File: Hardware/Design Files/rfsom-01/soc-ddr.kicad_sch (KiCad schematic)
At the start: 1 part

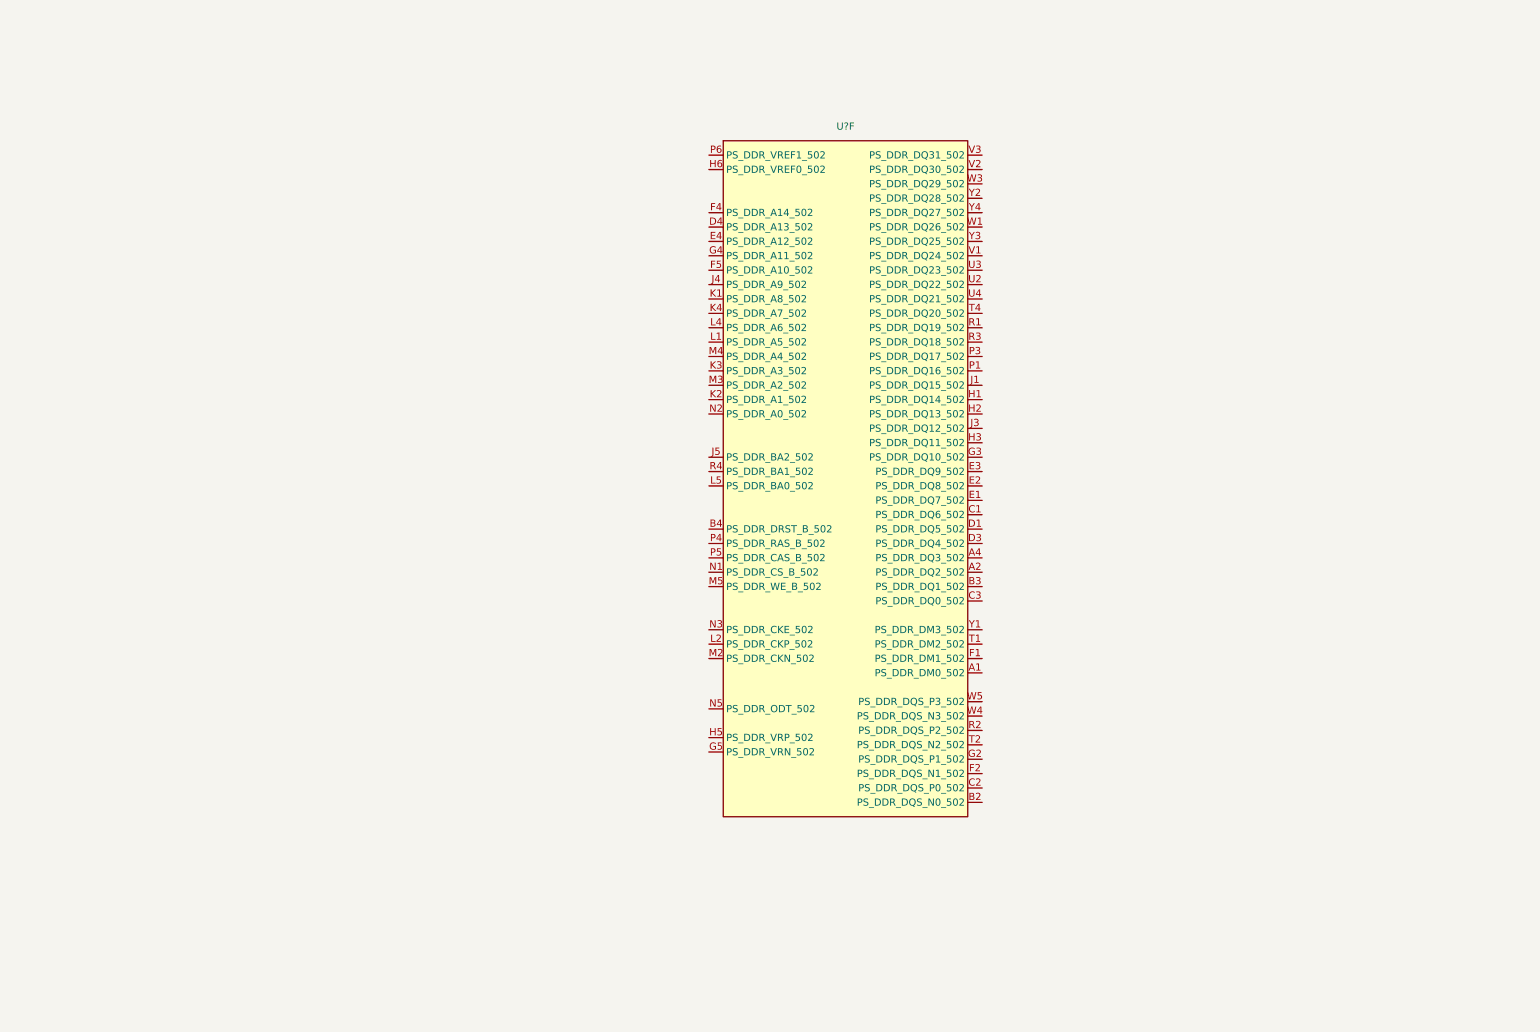
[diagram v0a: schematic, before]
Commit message: ddr progress; added more conns;
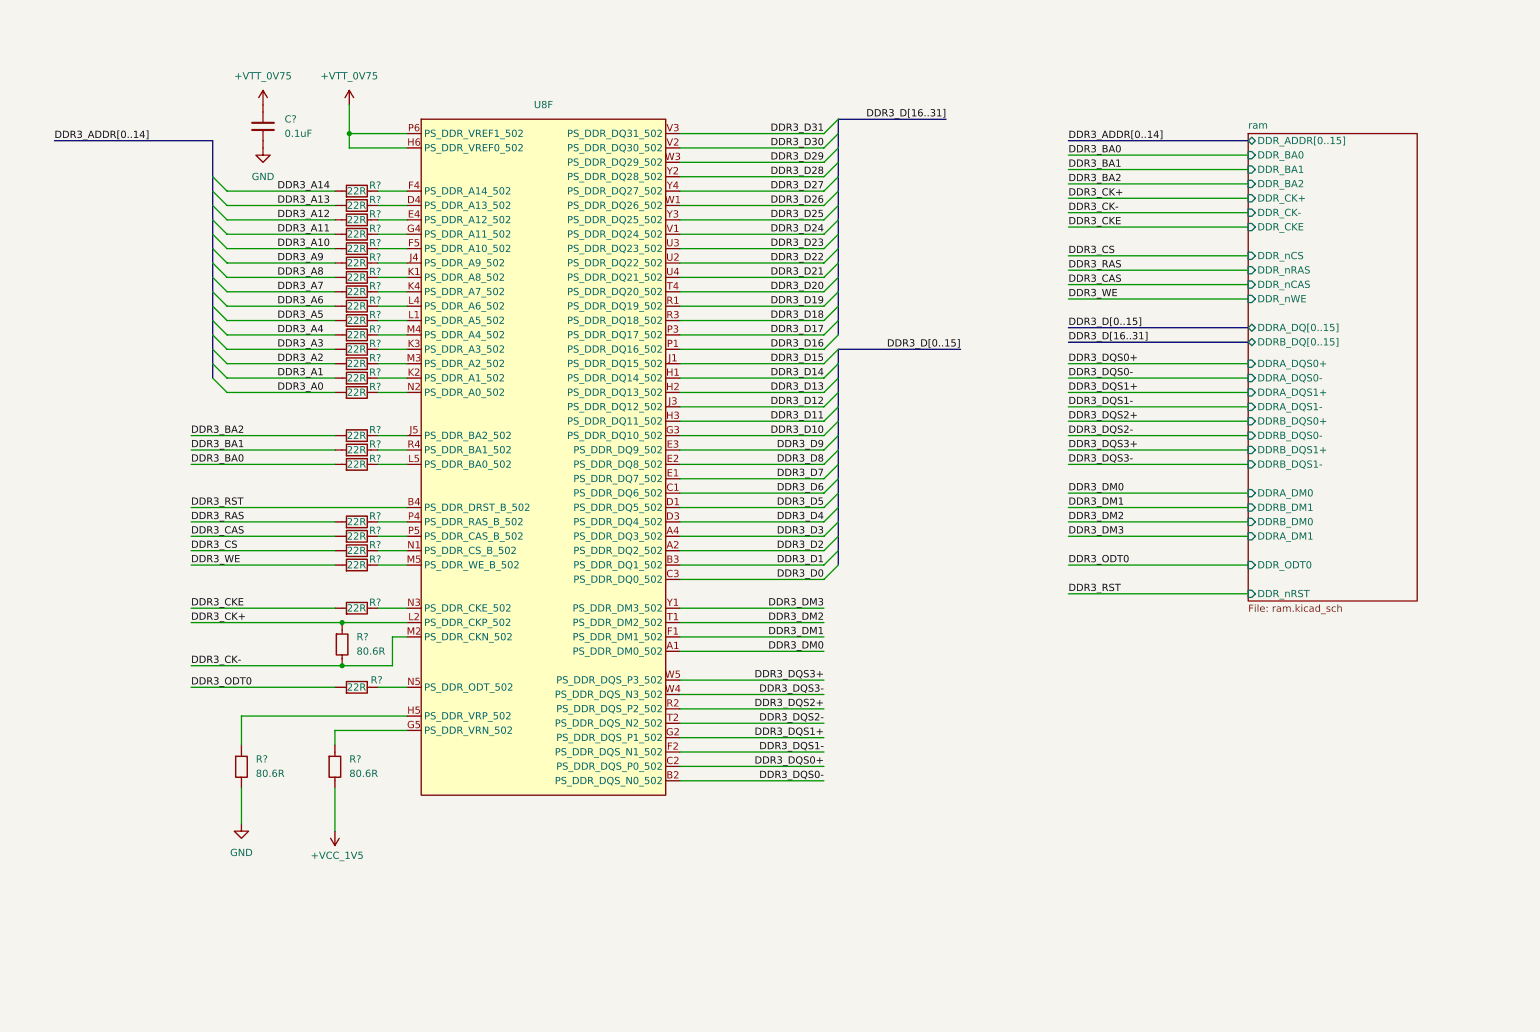
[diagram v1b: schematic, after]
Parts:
- added C?: CL05B104KA5NNNC, Capacitor_SMD:C_0402_1005Metric_Pad0.74x0.62mm_HandSolder, symbol Capacitors:CL05B104KA5NNNC
- added R? (x24): RC0402FR-0722RL, Resistor_SMD:R_0402_1005Metric, symbol Resistors:RC0402FR-0722RL
- added R? (x3): RC0402FR-0780R6L, Resistor_SMD:R_0402_1005Metric, symbol Resistors:RC0402FR-0780R6L
- U8: renamed from U?; footprint Package_BGA:Xilinx_CLG400 -> ICs:CLG400
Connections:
- net DDR3_DM0: now reaches U8.A1 (PS_DDR_DM0_502)
- net DDR3_D2: now reaches U8.A2 (PS_DDR_DQ2_502)
- net DDR3_D3: now reaches U8.A4 (PS_DDR_DQ3_502)
- net DDR3_DQS0-: now reaches U8.B2 (PS_DDR_DQS_N0_502)
- net DDR3_D1: now reaches U8.B3 (PS_DDR_DQ1_502)
- net DDR3_RST: now reaches U8.B4 (PS_DDR_DRST_B_502)
- net DDR3_D6: now reaches U8.C1 (PS_DDR_DQ6_502)
- net DDR3_DQS0+: now reaches U8.C2 (PS_DDR_DQS_P0_502)
- net DDR3_D0: now reaches U8.C3 (PS_DDR_DQ0_502)
- net DDR3_D5: now reaches U8.D1 (PS_DDR_DQ5_502)
- net DDR3_D4: now reaches U8.D3 (PS_DDR_DQ4_502)
- net at U8.D4 (PS_DDR_A13_502): now also R?.2
- net DDR3_D7: now reaches U8.E1 (PS_DDR_DQ7_502)
- net DDR3_D8: now reaches U8.E2 (PS_DDR_DQ8_502)
- net DDR3_D9: now reaches U8.E3 (PS_DDR_DQ9_502)
- net at U8.E4 (PS_DDR_A12_502): now also R?.2
- net DDR3_DM1: now reaches U8.F1 (PS_DDR_DM1_502)
- net DDR3_DQS1-: now reaches U8.F2 (PS_DDR_DQS_N1_502)
- net at U8.F4 (PS_DDR_A14_502): now also R?.2
- net at U8.F5 (PS_DDR_A10_502): now also R?.2
- net DDR3_DQS1+: now reaches U8.G2 (PS_DDR_DQS_P1_502)
- net DDR3_D10: now reaches U8.G3 (PS_DDR_DQ10_502)
- net at U8.G4 (PS_DDR_A11_502): now also R?.2
- net at U8.G5 (PS_DDR_VRN_502): now also R?.1
- net DDR3_D14: now reaches U8.H1 (PS_DDR_DQ14_502)
- net DDR3_D13: now reaches U8.H2 (PS_DDR_DQ13_502)
- net DDR3_D11: now reaches U8.H3 (PS_DDR_DQ11_502)
- net at U8.H5 (PS_DDR_VRP_502): now also R?.1
- net +VTT_0V75: now reaches U8.H6 (PS_DDR_VREF0_502)
- net +VTT_0V75: now also U8.P6 (PS_DDR_VREF1_502), C?.1
- net DDR3_D15: now reaches U8.J1 (PS_DDR_DQ15_502)
- net DDR3_D12: now reaches U8.J3 (PS_DDR_DQ12_502)
- net at U8.J4 (PS_DDR_A9_502): now also R?.2
- net at U8.J5 (PS_DDR_BA2_502): now also R?.2
- net at U8.K1 (PS_DDR_A8_502): now also R?.2
- net at U8.K2 (PS_DDR_A1_502): now also R?.2
- net at U8.K3 (PS_DDR_A3_502): now also R?.2
- net at U8.K4 (PS_DDR_A7_502): now also R?.2
- net at U8.L1 (PS_DDR_A5_502): now also R?.2
- net DDR3_CK+: now reaches U8.L2 (PS_DDR_CKP_502)
- net DDR3_CK+: now also R?.1
- net at U8.L4 (PS_DDR_A6_502): now also R?.2
- net at U8.L5 (PS_DDR_BA0_502): now also R?.2
- net DDR3_CK-: now reaches U8.M2 (PS_DDR_CKN_502)
- net DDR3_CK-: now also R?.2
- net at U8.M3 (PS_DDR_A2_502): now also R?.2
- net at U8.M4 (PS_DDR_A4_502): now also R?.2
- net at U8.M5 (PS_DDR_WE_B_502): now also R?.2
- net at U8.N1 (PS_DDR_CS_B_502): now also R?.2
- net at U8.N2 (PS_DDR_A0_502): now also R?.2
- net at U8.N3 (PS_DDR_CKE_502): now also R?.2
- net at U8.N5 (PS_DDR_ODT_502): now also R?.2
- net DDR3_D16: now reaches U8.P1 (PS_DDR_DQ16_502)
- net DDR3_D17: now reaches U8.P3 (PS_DDR_DQ17_502)
- net at U8.P4 (PS_DDR_RAS_B_502): now also R?.2
- net at U8.P5 (PS_DDR_CAS_B_502): now also R?.2
- net DDR3_D19: now reaches U8.R1 (PS_DDR_DQ19_502)
- net DDR3_DQS2+: now reaches U8.R2 (PS_DDR_DQS_P2_502)
- net DDR3_D18: now reaches U8.R3 (PS_DDR_DQ18_502)
- net at U8.R4 (PS_DDR_BA1_502): now also R?.2
- net DDR3_DM2: now reaches U8.T1 (PS_DDR_DM2_502)
- net DDR3_DQS2-: now reaches U8.T2 (PS_DDR_DQS_N2_502)
- net DDR3_D20: now reaches U8.T4 (PS_DDR_DQ20_502)
- net DDR3_D22: now reaches U8.U2 (PS_DDR_DQ22_502)
- net DDR3_D23: now reaches U8.U3 (PS_DDR_DQ23_502)
- net DDR3_D21: now reaches U8.U4 (PS_DDR_DQ21_502)
- net DDR3_D24: now reaches U8.V1 (PS_DDR_DQ24_502)
- net DDR3_D30: now reaches U8.V2 (PS_DDR_DQ30_502)
- net DDR3_D31: now reaches U8.V3 (PS_DDR_DQ31_502)
- net DDR3_D26: now reaches U8.W1 (PS_DDR_DQ26_502)
- net DDR3_D29: now reaches U8.W3 (PS_DDR_DQ29_502)
- net DDR3_DQS3-: now reaches U8.W4 (PS_DDR_DQS_N3_502)
- net DDR3_DQS3+: now reaches U8.W5 (PS_DDR_DQS_P3_502)
- net DDR3_DM3: now reaches U8.Y1 (PS_DDR_DM3_502)
- net DDR3_D28: now reaches U8.Y2 (PS_DDR_DQ28_502)
- net DDR3_D25: now reaches U8.Y3 (PS_DDR_DQ25_502)
- net DDR3_D27: now reaches U8.Y4 (PS_DDR_DQ27_502)
- new net +VCC_1V5: R?.2
- new net DDR3_A0: R?.1
- new net DDR3_A1: R?.1
- new net DDR3_A10: R?.1
- new net DDR3_A11: R?.1
- new net DDR3_A12: R?.1
- new net DDR3_A13: R?.1
- new net DDR3_A14: R?.1
- new net DDR3_A2: R?.1
- new net DDR3_A3: R?.1
- new net DDR3_A4: R?.1
- new net DDR3_A5: R?.1
- new net DDR3_A6: R?.1
- new net DDR3_A7: R?.1
- new net DDR3_A8: R?.1
- new net DDR3_A9: R?.1
- new net DDR3_BA0: R?.1
- new net DDR3_BA1: R?.1
- new net DDR3_BA2: R?.1
- new net DDR3_CAS: R?.1
- new net DDR3_CKE: R?.1
- new net DDR3_CS: R?.1
- new net DDR3_ODT0: R?.1
- new net DDR3_RAS: R?.1
- new net DDR3_WE: R?.1
- new net GND: C?.2, R?.2
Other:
- added sheet ram (ram.kicad_sch)
- moved on the sheet: U8F

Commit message: ps progress; added ftdi; mezz pinout pedinging;
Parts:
- added C? (x8): CL05B104KA5NNNC, Capacitor_SMD:C_0402_1005Metric_Pad0.74x0.62mm_HandSolder, symbol Capacitors:CL05B104KA5NNNC
- added C?: CL21B106KQQNFNE, Capacitor_SMD:C_0805_2012Metric, symbol Capacitors:CL21B106KQQNFNE
- added R? (x25): RT0402FRE0740R2L, Resistor_SMD:R_0402_1005Metric, symbol Resistors:RT0402FRE0740R2L
- added R?: RES_01, Resistor_SMD:R_0402_1005Metric, symbol Resistors:RC0402FR-074K7L
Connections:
- net +VCC_1V5: now also R?.1
- net +VTT_0V75: now also C?.1, C?.1, C?.1, C?.1, C?.1, C?.1, C?.1, C?.1, C?.1, R?.1, R?.1, R?.1, R?.1, R?.1, R?.1, R?.1, R?.1, R?.1, R?.1, R?.1, R?.1, R?.1, R?.1, R?.1, R?.1, R?.1, R?.1, R?.1, R?.1, R?.1, R?.1, R?.1, R?.1
- net DDR3_A0: now also R?.2
- net DDR3_A1: now also R?.2
- net DDR3_A10: now also R?.2
- net DDR3_A11: now also R?.2
- net DDR3_A12: now also R?.2
- net DDR3_A13: now also R?.2
- net DDR3_A14: now also R?.2
- net DDR3_A2: now also R?.2
- net DDR3_A3: now also R?.2
- net DDR3_A4: now also R?.2
- net DDR3_A5: now also R?.2
- net DDR3_A6: now also R?.2
- net DDR3_A7: now also R?.2
- net DDR3_A8: now also R?.2
- net DDR3_A9: now also R?.2
- net DDR3_CKE: now also R?.2
- net DDR3_RST: now also R?.1
- net GND: now also C?.2, C?.2, C?.2, C?.2, C?.2, C?.2, C?.2, C?.2, C?.2, R?.2
- new net DDR_BA0: R?.2
- new net DDR_BA1: R?.2
- new net DDR_BA2: R?.2
- new net DDR_CKE: R?.2
- new net DDR_ODT0: R?.2
- new net DDR_nCAS: R?.2
- new net DDR_nCS: R?.2
- new net DDR_nRAS: R?.2
- new net DDR_nWE: R?.2
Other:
- sheet ram ports: added DDRA_DM[0..1], DDRB_DM[0..1], DDR_ADDR[0..14], DDR_BA[0..2]; removed DDRA_DM0, DDRA_DM1, DDRB_DM0, DDRB_DM1, DDR_ADDR[0..15], DDR_BA0, DDR_BA1, DDR_BA2
- moved on the sheet: C?, R?, U8F

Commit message: some ddr routing progress; layerstack per pcbway standard options, review reqd; commit prior to ddr split;
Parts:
- C112, C113, C114, C115, C116, C117, C118, C119, C120: renamed from C?; footprint Capacitor_SMD:C_0402_1005Metric_Pad0.74x0.62mm_HandSolder -> Capacitor_SMD:C_0402_1005Metric
- gave numbers to parts that had none: 54
- renumbered U8 to U5
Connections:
- net DDR3_A0: now also R109.2, U5.N2 (PS_DDR_A0_502); no longer R109.1, R77.2
- net DDR3_A1: now also R108.2, U5.K2 (PS_DDR_A1_502); no longer R108.1, R78.2
- net DDR3_A10: now also R99.2, U5.F5 (PS_DDR_A10_502); no longer R87.2, R99.1
- net DDR3_A11: now also R98.2, U5.G4 (PS_DDR_A11_502); no longer R88.2, R98.1
- net DDR3_A12: now also R97.2, U5.E4 (PS_DDR_A12_502); no longer R89.2, R97.1
- net DDR3_A13: now also R96.2, U5.D4 (PS_DDR_A13_502); no longer R90.2, R96.1
- net DDR3_A14: now also R95.2, U5.F4 (PS_DDR_A14_502); no longer R91.2, R95.1
- net DDR3_A2: now also R107.2, U5.M3 (PS_DDR_A2_502); no longer R107.1, R79.2
- net DDR3_A3: now also R106.2, U5.K3 (PS_DDR_A3_502); no longer R106.1, R80.2
- net DDR3_A4: now also R105.2, U5.M4 (PS_DDR_A4_502); no longer R105.1, R81.2
- net DDR3_A5: now also R104.2, U5.L1 (PS_DDR_A5_502); no longer R104.1, R82.2
- net DDR3_A6: now also R103.2, U5.L4 (PS_DDR_A6_502); no longer R103.1, R83.2
- net DDR3_A7: now also R102.2, U5.K4 (PS_DDR_A7_502); no longer R102.1, R84.2
- net DDR3_A8: now also R101.2, U5.K1 (PS_DDR_A8_502); no longer R101.1, R85.2
- net DDR3_A9: now also R100.2, U5.J4 (PS_DDR_A9_502); no longer R100.1, R86.2
- new net DDR3_ADDR0: R109.1, R77.2
- new net DDR3_ADDR1: R108.1, R78.2
- new net DDR3_ADDR10: R87.2, R99.1
- new net DDR3_ADDR11: R88.2, R98.1
- new net DDR3_ADDR12: R89.2, R97.1
- new net DDR3_ADDR13: R90.2, R96.1
- new net DDR3_ADDR14: R91.2, R95.1
- new net DDR3_ADDR2: R107.1, R79.2
- new net DDR3_ADDR3: R106.1, R80.2
- new net DDR3_ADDR4: R105.1, R81.2
- new net DDR3_ADDR5: R104.1, R82.2
- new net DDR3_ADDR6: R103.1, R83.2
- new net DDR3_ADDR7: R102.1, R84.2
- new net DDR3_ADDR8: R101.1, R85.2
- new net DDR3_ADDR9: R100.1, R86.2
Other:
- moved on the sheet: R100, R101, R102, R103, R104, R105, R106, R107, R108, R109, R95, R96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

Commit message: added starage, usb sch; more design progress in sch;
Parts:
- R100, R101, R102, R103, R104, R105, R106, R107, R108, R109, R110, R111, R112, R113, R114, R115, R116, R117, R118, R95, R96, R97, R98, R99: footprint Resistor_SMD:R_0402_1005Metric -> Resistor_SMD:R_0603_1608Metric; symbol Resistors:RC0402FR-0722RL -> Resistors:RC0603FR-0749R9L; Resistance 22R -> 49.9R
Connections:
- net DDR_BA0 is gone; now on net DDR3_BA0: R76.2
- net DDR_BA1 is gone; now on net DDR3_BA1: R75.2
- net DDR_BA2 is gone; now on net DDR3_BA2: R74.2
- net DDR_CKE is gone; now on net DDR3_CKE: R73.2
- net DDR_ODT0 is gone; now on net DDR3_ODT0: R68.2
- net DDR_nCAS is gone; now on net DDR3_nCAS: R70.2
- net DDR_nCS is gone; now on net DDR3_nCS: R72.2
- net DDR_nRAS is gone; now on net DDR3_nRAS: R71.2
- net DDR_nWE is gone; now on net DDR3_nWE: R69.2
- net at R94.1: no longer U5.H5 (PS_DDR_VRP_502)
- net at R120.1: no longer U5.G5 (PS_DDR_VRN_502)
- net at U5.N5 (PS_DDR_ODT_502): no longer R118.2
- net +VCC_1V5 renamed +PS_VCC_1V5
- net +VTT_0V75 renamed +PS_VTT_0V75
- net DDR3_CAS renamed DDR3_nCAS
- net DDR3_CS renamed DDR3_nCS
- net DDR3_RAS renamed DDR3_nRAS
- net DDR3_WE renamed DDR3_nWE
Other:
- sheet ram renamed ram-ps_b1
- added sheet ram-ps_b2 (ram.kicad_sch)
- sheet ram-ps_b1 ports: added none; removed DDRB_DM[0..1], DDRB_DQS0+, DDRB_DQS0-, DDRB_DQS1+, DDRB_DQS1-, DDRB_DQ[0..15]
- note added: "!"
- moved on the sheet: C120, R100, R101, R102, R103, R104, R105, R106, R107, R108, R109, R110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
